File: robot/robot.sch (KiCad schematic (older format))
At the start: 3 parts

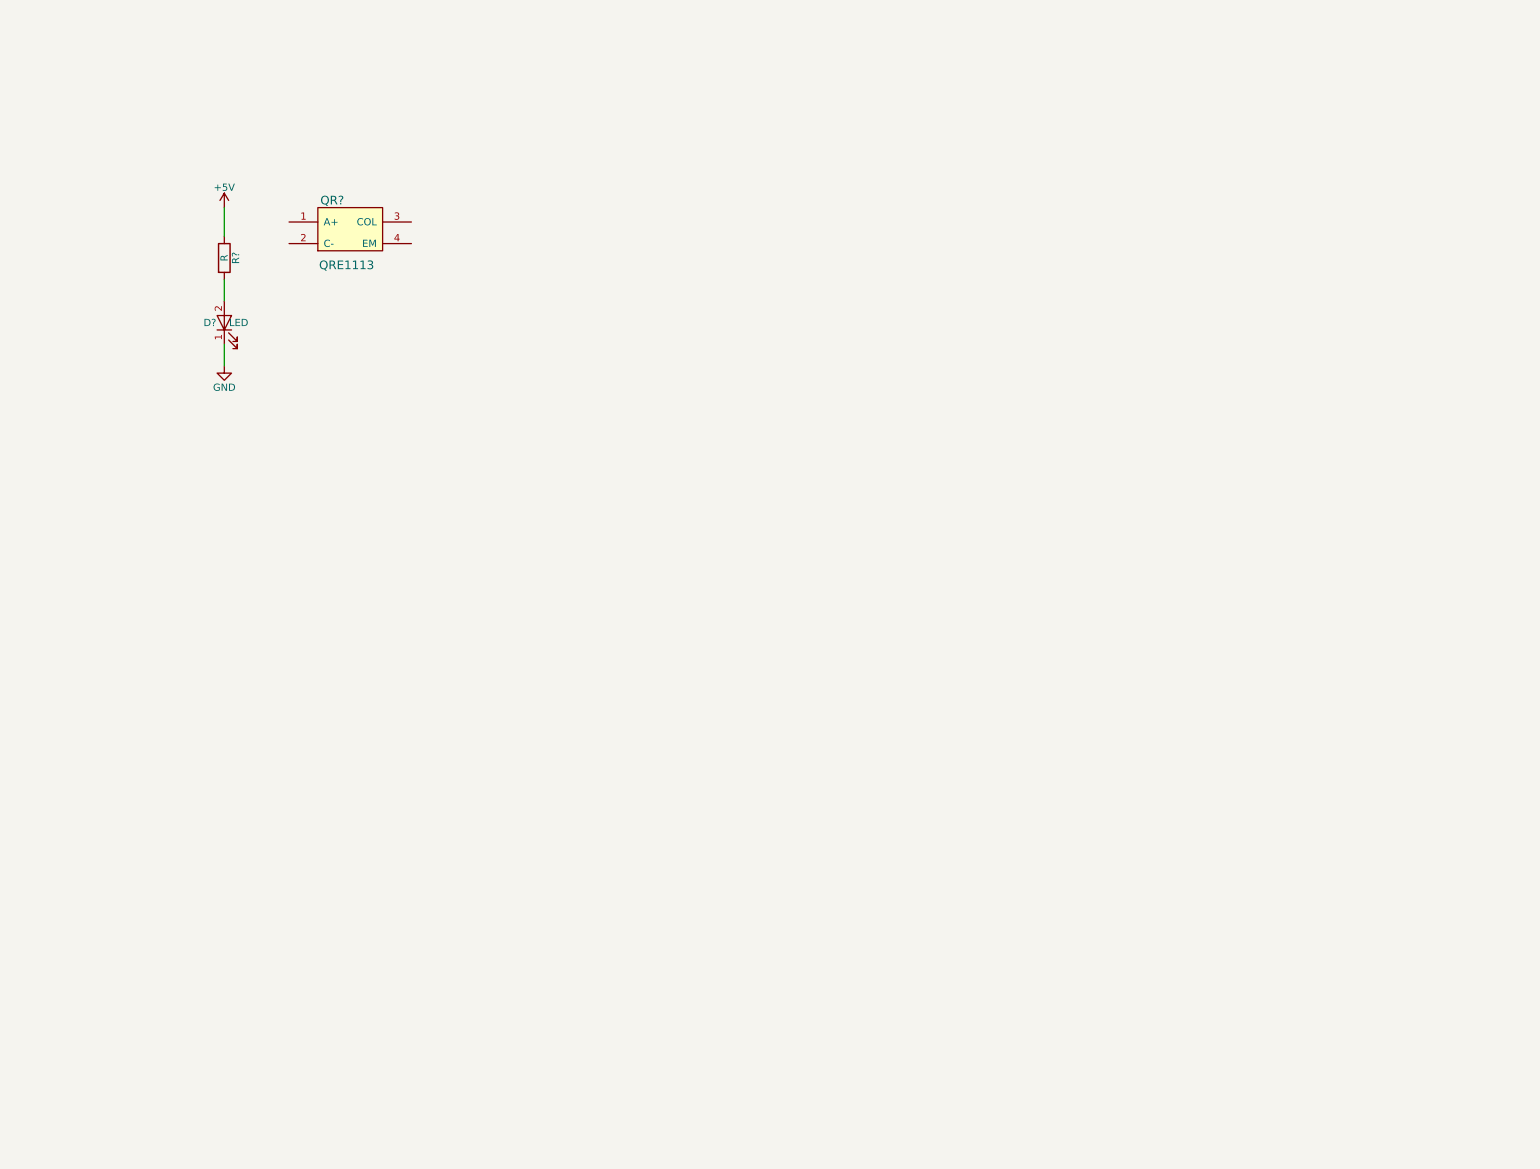
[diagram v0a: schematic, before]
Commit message: starting schematics
Done few first steps
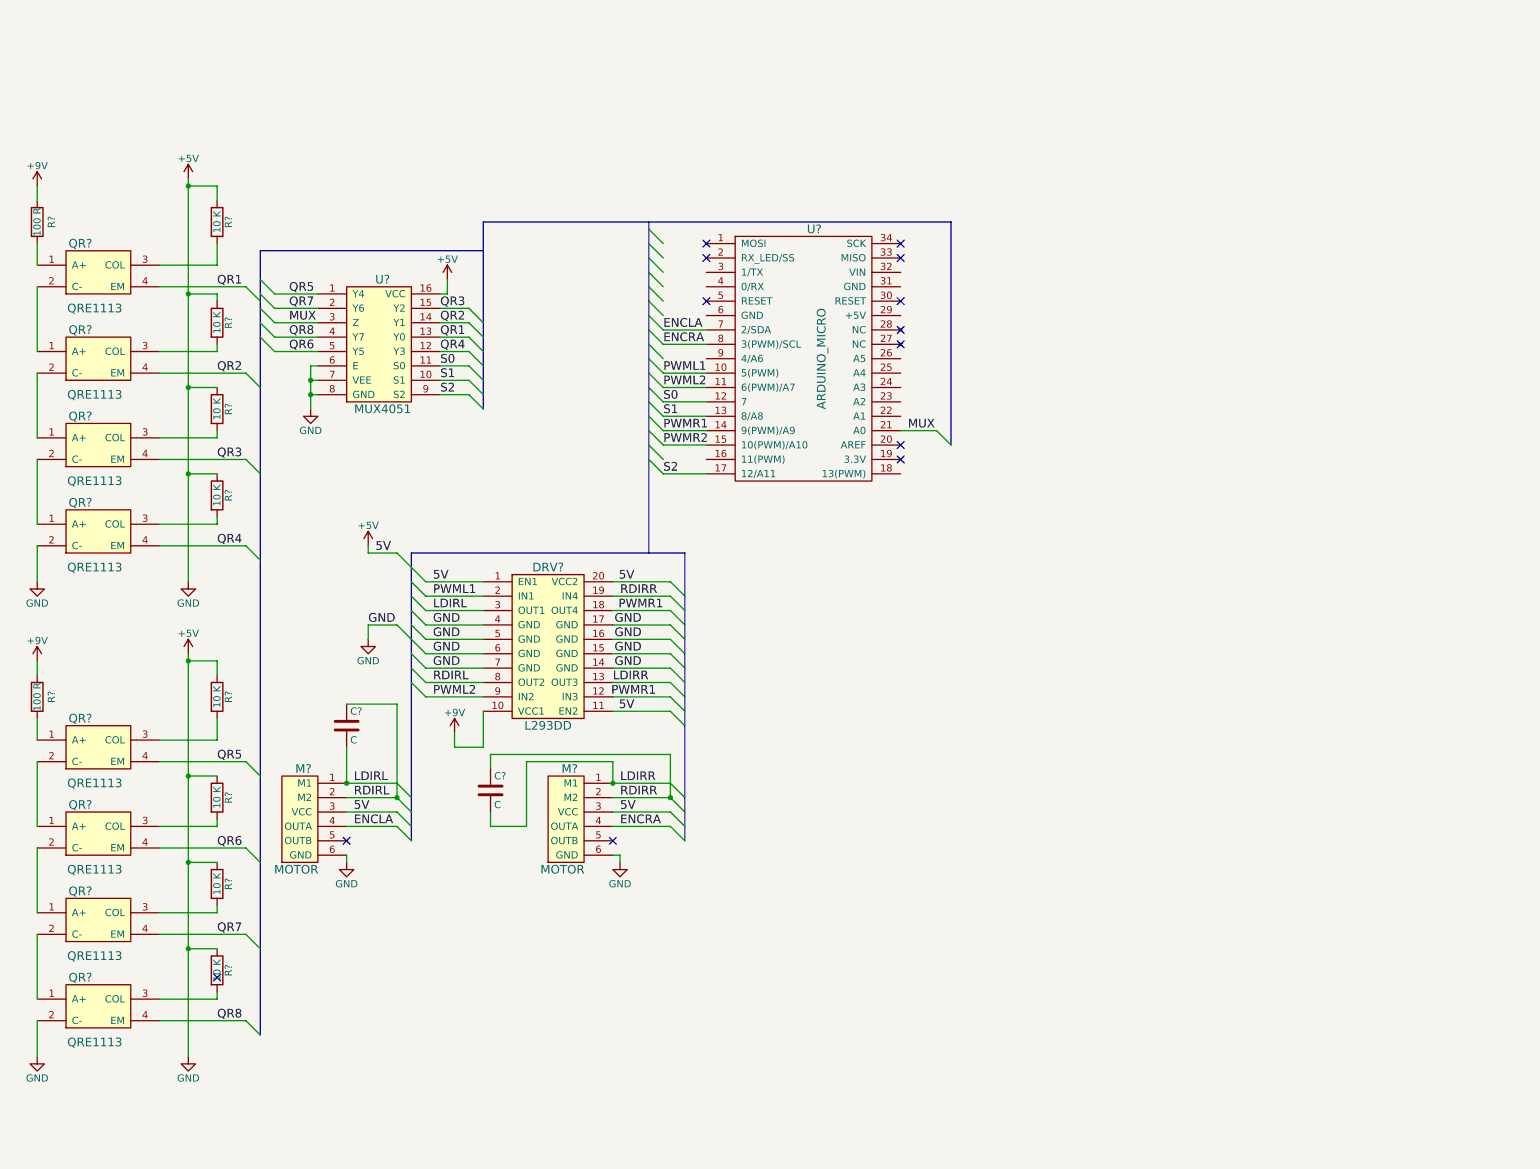
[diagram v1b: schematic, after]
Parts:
- removed D?: LED, symbol LED
- removed QR?: QRE1113, symbol QRE1113
- removed R?: R, symbol R
- added C? (x2): C, symbol C
- added DRV?: L293DD, symbol L293DD
- added M? (x2): MOTOR, symbol MOTOR
- added QR? (x8): QRE1113, symbol QRE1113
- added R? (x2): 100 R, symbol R
- added R? (x8): 10 K, symbol R
- added U?: ARDUINO_MICRO, symbol ARDUINO_MICRO_SHIELD
- added U?: MUX4051, symbol MUX4051
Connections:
- net +5V: now also DRV?.1 (EN1), DRV?.11 (EN2), DRV?.14 (GND), DRV?.15 (GND), DRV?.16 (GND), DRV?.17 (GND), DRV?.20 (VCC2), DRV?.4 (GND), DRV?.5 (GND), DRV?.6 (GND), DRV?.7 (GND), M?.3 (VCC), M?.3 (VCC), M?.6 (GND), M?.6 (GND), QR?.2 (C-), QR?.2 (C-), R?.1, R?.1, R?.1, R?.1, R?.1, R?.1, R?.1, R?.1, U?.16 (VCC), U?.6 (E), U?.7 (VEE), U?.8 (GND)
- new net: QR?.1 (A+), R?.2 (x2)
- new net: QR?.1 (A+), QR?.2 (C-) (x6)
- new net: QR?.3 (COL), R?.2 (x8)
- new net +9V: DRV?.10 (VCC1), R?.1, R?.1
- new net ENCLA: M?.4 (OUTA), U?.7 (2/SDA)
- new net ENCRA: M?.4 (OUTA), U?.8 (3(PWM)/SCL)
- new net LDIRL: C?.2, DRV?.3 (OUT1), M?.1 (M1)
- new net LDIRR: C?.2, DRV?.13 (OUT3), M?.1 (M1)
- new net MUX: U?.21 (A0), U?.3 (Z)
- new net PWML1: DRV?.2 (IN1), U?.10 (5(PWM))
- new net PWML2: DRV?.9 (IN2), U?.11 (6(PWM)/A7)
- new net PWMR1: DRV?.12 (IN3), DRV?.18 (OUT4), U?.14 (9(PWM)/A9)
- new net PWMR2: U?.15 (10(PWM)/A10)
- new net QR1: QR?.4 (EM), U?.13 (Y0)
- new net QR2: QR?.4 (EM), U?.14 (Y1)
- new net QR3: QR?.4 (EM), U?.15 (Y2)
- new net QR4: QR?.4 (EM), U?.12 (Y3)
- new net QR5: QR?.4 (EM), U?.1 (Y4)
- new net QR6: QR?.4 (EM), U?.5 (Y5)
- new net QR7: QR?.4 (EM), U?.2 (Y6)
- new net QR8: QR?.4 (EM), U?.4 (Y7)
- new net RDIRL: C?.1, DRV?.8 (OUT2), M?.2 (M2)
- new net RDIRR: C?.1, DRV?.19 (IN4), M?.2 (M2)
- new net S0: U?.11 (S0), U?.12 (7)
- new net S1: U?.10 (S1), U?.13 (8/A8)
- new net S2: U?.17 (12/A11), U?.9 (S2)
- no-connect marks 0 -> 13

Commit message: upgrading scheme
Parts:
- added BT?: RN-42, symbol RN-42
- added R?: 5 K, symbol R
- added R?: 10 K, symbol R
- M?: value MOTOR -> MOTOR LEVI
- M?: value MOTOR -> MOTOR DESNI
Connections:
- net +5V: now also U?.31 (GND), BT?.12 (GND), R?.2
- net at U?.19 (3.3V): now also BT?.11 (VDD)
- net TX: now reaches U?.3 (1/TX)
- net TX: now also R?.1
- net RX: now reaches U?.4 (0/RX)
- net RX: now also BT?.14 (UART_TX)
- new net: BT?.13 (UART_RX), R?.1, R?.2
- no-connect marks 13 -> 40
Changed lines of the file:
@@
 $EndComp
-Entry Wire Line
-	5100 1250 5200 1350
-Entry Wire Line
-	5100 1350 5200 1450
 Entry Wire Line
 	5100 1450 5200 1550
 Entry Wire Line
 	5100 1550 5200 1650
-Entry Wire Line
-	5100 1650 5200 1750
 Entry Wire Line
 	5100 1750 5200 1850
@@
 P 2550 5700
 F 0 "M?" H 2700 6400 60  0000 C CNN
-F 1 "MOTOR" H 2650 5700 60  0000 C CNN
+F 1 "MOTOR LEVI" H 2650 5700 60  0000 C CNN
 F 2 "" H 2500 5900 60  0001 C CNN
 F 3 "" H 2500 5900 60  0001 C CNN
@@
 P 4400 5700
 F 0 "M?" H 4550 6400 60  0000 C CNN
-F 1 "MOTOR" H 4500 5700 60  0000 C CNN
+F 1 "MOTOR DESNI" H 4500 5700 60  0000 C CNN
 F 2 "" H 4350 5900 60  0001 C CNN
 F 3 "" H 4350 5900 60  0001 C CNN
@@
 NoConn ~ 6850 2050
 NoConn ~ 6850 2750
-NoConn ~ 6850 2850
 NoConn ~ 5500 1350
 NoConn ~ 5500 1450
@@
 Text Label 5200 2050 0    60   ~ 0
 ENCRA
+Entry Wire Line
+	7100 1650 7200 1750
+Entry Wire Line
+	7100 1850 7200 1950
+Text Label 7100 1650 2    60   ~ 0
+GND
+$Comp
+L RN-42 BT?
+U 1 1 58B76B30
+P 7450 3450
+F 0 "BT?" H 8150 5450 60  0000 C CNN
+F 1 "RN-42" H 8150 3550 60  0000 C CNN
+F 2 "" H 7450 4150 60  0001 C CNN
+F 3 "" H 7450 4150 60  0001 C CNN
+	1    7450 3450
+	1    0    0    -1
+$EndComp
+Entry Wire Line
+	9050 2600 9150 2700
 Wire Wire Line
 	850  950  850  1050
@@
 	3650 2100 3850 2100
 Wire Bus Line
-	3950 1200 7200 1200
+	3950 1200 9150 1200
 Wire Wire Line
 	2800 2200 2750 2200
@@
 Wire Wire Line
 	5500 1950 5200 1950
+Wire Wire Line
+	5500 1550 5200 1550
+Wire Wire Line
+	5500 1650 5200 1650
+Wire Wire Line
+	5500 1850 5200 1850
+Wire Wire Line
+	7100 1650 6850 1650
+Wire Wire Line
+	7100 1850 6850 1850
+Wire Bus Line
+	9150 1200 9150 2800
+Wire Wire Line
+	9050 2600 8800 2600
+Text Label 5200 1650 0    60   ~ 0
+RX
+Text Label 8900 2600 0    60   ~ 0
+RX
+$Comp
+L R R?
+U 1 1 58B7881F
+P 8900 2950
+F 0 "R?" V 8980 2950 50  0000 C CNN
+F 1 "5 K" V 8900 2950 50  0000 C CNN
+F 2 "" V 8830 2950 50  0000 C CNN
+F 3 "" H 8900 2950 50  0000 C CNN
+	1    8900 2950
+	0    1    1    0
+$EndComp
+$Comp
+L R R?
+U 1 1 58B790EB
+P 8750 3100
+F 0 "R?" V 8850 3100 50  0000 C CNN
+F 1 "10 K" V 8750 3100 50  0000 C CNN
+F 2 "" V 8680 3100 50  0000 C CNN
+F 3 "" H 8750 3100 50  0000 C CNN
+	1    8750 3100
+	1    0    0    -1
+$EndComp
+Entry Wire Line
+	9050 2700 9150 2800
+Text Label 5200 1550 0    60   ~ 0
+TX
+Text Label 8900 2700 0    60   ~ 0
+TX
+$Comp
+L GND #PWR?
+U 1 1 58B7B164
+P 8750 3250
+F 0 "#PWR?" H 8750 3000 50  0001 C CNN
+F 1 "GND" H 8750 3100 50  0000 C CNN
+F 2 "" H 8750 3250 50  0000 C CNN
+F 3 "" H 8750 3250 50  0000 C CNN
+	1    8750 3250
+	1    0    0    -1
+$EndComp
+Wire Wire Line
+	8800 2700 8800 2800
+Wire Wire Line
+	8800 2800 8750 2800
+Wire Wire Line
+	8750 2800 8750 2950
+Wire Wire Line
+	9050 2950 9050 2800
+Wire Wire Line
+	9050 2800 8900 2800
+Wire Wire Line
+	8900 2800 8900 2700
+Wire Wire Line
+	8900 2700 9050 2700
+Entry Wire Line
+	7200 2600 7300 2700
+Wire Wire Line
+	7300 2700 7450 2700
+Text Label 7300 2700 0    60   ~ 0
+GND
+NoConn ~ 7450 1600
+NoConn ~ 7450 1700
+NoConn ~ 7450 1800
+NoConn ~ 7450 1900
+NoConn ~ 7450 2000
+NoConn ~ 7450 2100
+NoConn ~ 7450 2200
+NoConn ~ 7450 2300
+NoConn ~ 7450 2400
+NoConn ~ 7450 2500
+NoConn ~ 8800 1600
+NoConn ~ 8800 1700
+NoConn ~ 8800 1800
+NoConn ~ 8800 1900
+NoConn ~ 8800 2000
+NoConn ~ 8800 2100
+NoConn ~ 8800 2200
+NoConn ~ 8800 2300
+NoConn ~ 8800 2400
+NoConn ~ 8800 2500
+NoConn ~ 8500 3250
+NoConn ~ 8400 3250
+NoConn ~ 8300 3250
+NoConn ~ 8200 3250
+NoConn ~ 8100 3250
+NoConn ~ 8000 3250
+NoConn ~ 7900 3250
+NoConn ~ 7800 3250
+Wire Wire Line
+	6850 2850 7250 2850
+Wire Wire Line
+	7250 2850 7250 2600
+Wire Wire Line
+	7250 2600 7450 2600
 $EndSCHEMATC

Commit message: submiting sheme
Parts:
- added BT1: Battery_Cell, symbol Battery_Cell
- added Q1: Q_NPN_CBE, symbol Q_NPN_CBE
- added VREG1: UA78M33, symbol UA78M33
- added XOR1: SN74LS86AD, symbol SN74LS86AD
- gave numbers to parts that had none: 28
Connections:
- net +5V: now also U2.29 (+5V), BT1.2 (-), Q1.3 (E), VREG1.2 (C), VREG1.4 (C), XOR1.14 (VCC), XOR1.7 (GND); no longer QR4.2 (C-), QR8.2 (C-)
- net +9V: now also U2.32 (VIN), BT1.1 (+), VREG1.1 (IN)
- net ENCLA: now also U2.25 (A4), XOR1.1 (1A); no longer U2.7 (2/SDA)
- net ENCRA: now also U2.24 (A3), XOR1.4 (2A); no longer U2.8 (3(PWM)/SCL)
- net ENCLB: now reaches M1.5 (OUTB)
- net ENCLB: now also U2.9 (4/A6), XOR1.2 (1B)
- net ENCRB: now reaches M2.5 (OUTB)
- net ENCRB: now also U2.16 (11(PWM)), XOR1.5 (2B)
- net at U2.19 (3.3V): no longer BTH1.11 (VDD)
- net LON: now reaches U2.26 (A5)
- net LON: now also Q1.2 (B)
- new net: Q1.1 (C), QR4.2 (C-), QR8.2 (C-)
- new net: BTH1.11 (VDD), VREG1.3 (OUT)
- new net LXOR: U2.7 (2/SDA), XOR1.3 (1Y)
- new net RXOR: U2.8 (3(PWM)/SCL), XOR1.6 (2Y)
- no-connect marks 40 -> 48
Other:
- moved on the sheet: BTH1, C1, C2, DRV1, M1, M2, QR1, QR2, QR3, QR4, QR5, QR6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

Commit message: PCB design
Adding pcb design with footprints with few 3D models.
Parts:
- added R13: 1K, Resistors_SMD:R_0805_HandSoldering, symbol R
- added SW1: JSA4-1-G0, footprints_robot:JSA4-1-G0, symbol JSA4-1-G0
- BT1: footprint (none) -> footprints_robot:battery_holder
- BTH1: footprint (none) -> RN-42-HID-RD1:MICROCHIP_RN-42-HID-RD1
- C1, C2: footprint (none) -> Capacitors_SMD:C_0805_HandSoldering
- DRV1: footprint (none) -> footprints_robot:L293DD
- M1, M2: footprint (none) -> footprints_robot:EM_Encoder
- Q1: footprint (none) -> footprints_robot:BSV52_NPN
- QR1, QR2, QR3, QR4, QR5, QR6, QR7, QR8: footprint (none) -> footprints_robot:QRE1113GR
- R1, R10, R11, R12, R2, R3, R4, R5, R6, R7, R8, R9: footprint (none) -> Resistors_SMD:R_0805_HandSoldering
- U1: footprint (none) -> SOP63P600X175-16N:SOP63P600X175-16N
- U2: footprint (none) -> footprints_robot:ARDUINO_MICRO_SHIELD
- VREG1: footprint (none) -> footprints_robot:UA78M33-Q1_DCY_4
- XOR1: footprint (none) -> SOIC127P600X175-14N:SOIC127P600X175-14N
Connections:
- net +5V: no longer BT1.2 (-), BTH1.12 (GND), DRV1.14 (GND), DRV1.15 (GND), DRV1.16 (GND), DRV1.17 (GND), DRV1.4 (GND), DRV1.5 (GND), DRV1.6 (GND), DRV1.7 (GND), M1.6 (GND), M2.6 (GND), Q1.3 (E), R11.2, U1.6 (E), U1.7 (VEE), U1.8 (GND), U2.31 (GND), VREG1.2 (C), VREG1.4 (C), XOR1.7 (GND)
- net +9V: now also SW1.1 (IN); no longer BT1.1 (+)
- net LON: now also R13.1; no longer Q1.2 (B)
- net QR1: now also QR1.3 (COL), R3.2; no longer QR1.4 (EM)
- net QR2: now also QR2.3 (COL), R4.2; no longer QR2.4 (EM)
- net QR3: now also QR3.3 (COL), R5.2; no longer QR3.4 (EM)
- net QR4: now also QR4.3 (COL), R6.2; no longer QR4.4 (EM)
- net QR5: now also QR5.3 (COL), R7.2; no longer QR5.4 (EM)
- net QR6: now also QR6.3 (COL), R8.2; no longer QR6.4 (EM)
- net QR7: now also QR7.3 (COL), R9.2; no longer QR7.4 (EM)
- net QR8: now also QR8.3 (COL), R10.2; no longer QR8.4 (EM)
- net GND: now reaches U2.6 (GND)
- net GND: now also BT1.2 (-), BTH1.12 (GND), DRV1.14 (GND), DRV1.15 (GND), DRV1.16 (GND), DRV1.17 (GND), DRV1.4 (GND), DRV1.5 (GND), DRV1.6 (GND), DRV1.7 (GND), M1.6 (GND), M2.6 (GND), Q1.3 (E), QR1.4 (EM), QR2.4 (EM), QR3.4 (EM), QR4.4 (EM), QR5.4 (EM), QR6.4 (EM), QR7.4 (EM), QR8.4 (EM), R11.2, U1.6 (E), U1.7 (VEE), U1.8 (GND), U2.31 (GND), VREG1.2 (C), VREG1.4 (C), XOR1.7 (GND)
- new net: Q1.2 (B), R13.2
- new net: BT1.1 (+), SW1.2 (OUT)
- no-connect marks 48 -> 47
